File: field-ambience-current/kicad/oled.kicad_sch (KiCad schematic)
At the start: 7 parts, among them J1 USB_C_Receptacle (TYPE-C-31-M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

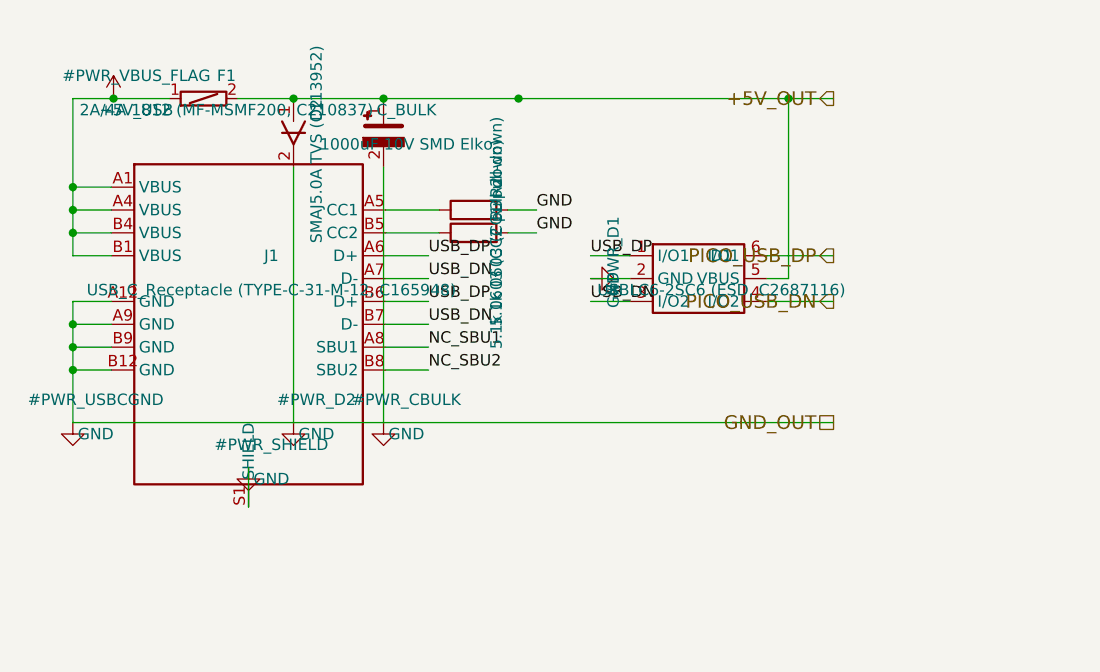
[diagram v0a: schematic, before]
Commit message: Add Sheet 3 (OLED) per SPEC v0.6 §6
J3 16-pin header für ER-OLEDM032-1W 256x64 SSD1322 OLED-Modul:
- Pin 1 VSS → GND
- Pin 2 VBAT → +5V mit lokalem C6b 10µF + C6c 100nF (250mA peak)
- Pin 3 VDD → +3V3 mit lokalem C6 100nF (Logic)
- Pin 4, 14-16 NC (Labels gegen Dangling-Wire-Warnings)
- Pin 5 BS1, Pin 6 BS0 → GND (4-wire SPI mode)
- Pin 7 RES#, Pin 8 CS#, Pin 9 DC# → OLED_RES/CS/DC (Pico GP9/5/8)
- Pin 10 E/RW, Pin 11 RW/E → GND (4-wire SPI unused)
- Pin 12 SCLK, Pin 13 SDIN → OLED_SCK/MOSI (Pico GP6/7)

Root sheet erweitert mit OLED sheet pin + inter-sheet SPI bus wires
zwischen Pico und OLED (SCK/MOSI/CS/DC/RES).

Generic Conn_01x16 lib_symbol generator added.

Analyzer: 0 errors, 30 warnings (down from 35), 20 components total.
All J3 pin_nets verified correct via analyzer pin_nets dump.
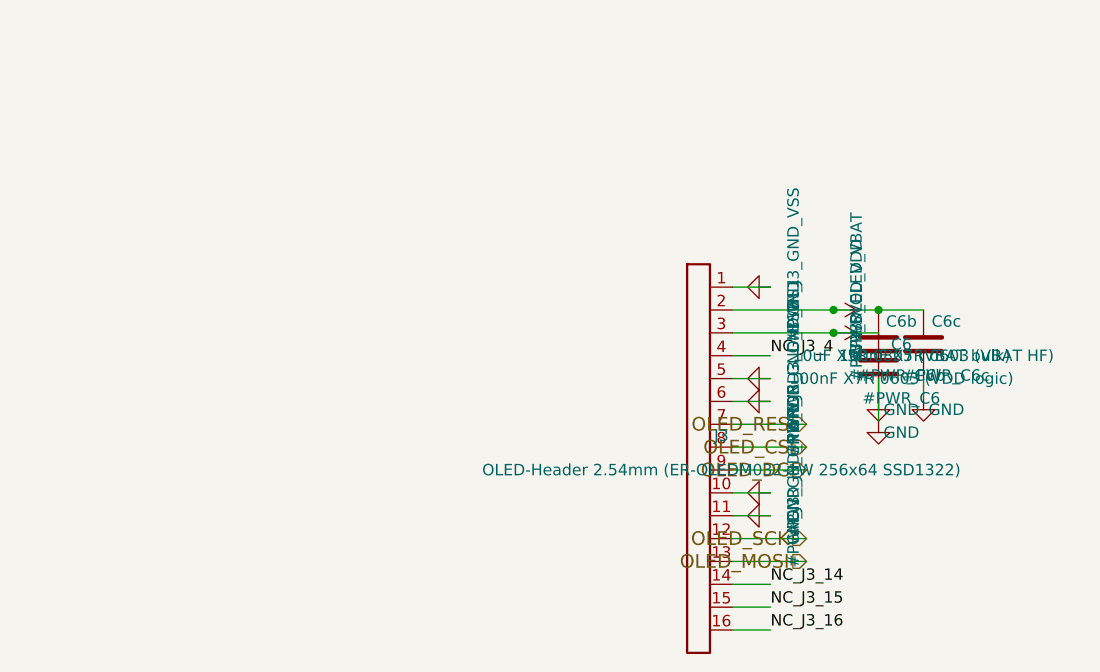
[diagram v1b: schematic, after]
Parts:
- removed C_BULK: 1000uF 10V SMD Elko, Capacitor_SMD:CP_Elec_8x6.7, symbol Device:CP
- removed D1: USBLC6-2SC6 (ESD, C2687116), Package_TO_SOT_SMD:SOT-23-6, symbol Power_Protection:USBLC6-2SC6
- removed D2: SMAJ5.0A TVS (C113952), Diode_SMD:D_SMA, symbol Device:D_TVS
- removed F1: 2A/4A 1812 (MF-MSMF200, C210837), Fuse:Fuse_1812_4532Metric, symbol Device:Polyfuse
- removed J1: USB_C_Receptacle (TYPE-C-31-M-12, C165948), Connector_USB:USB_C_Receptacle_HRO_TYPE-C-31-M-12, symbol Connector:USB_C_Receptacle
- removed R2: 5.1k 0603 (CC1 pull-down), Resistor_SMD:R_0603_1608Metric, symbol Device:R
- removed R3: 5.1k 0603 (CC2 pull-down), Resistor_SMD:R_0603_1608Metric, symbol Device:R
- added C6: 100nF X7R 0603 (VDD logic), Capacitor_SMD:C_0603_1608Metric, symbol Device:C
- added C6b: 10uF X5R 0805 (VBAT bulk), Capacitor_SMD:C_0805_2012Metric, symbol Device:C
- added C6c: 100nF X7R 0603 (VBAT HF), Capacitor_SMD:C_0603_1608Metric, symbol Device:C
- added J3: OLED-Header 2.54mm (ER-OLEDM032-1W 256x64 SSD1322), Connector_PinHeader_2.54mm:PinHeader_1x16_P2.54mm_Vertical, symbol Connector:Conn_01x16
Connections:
- net GND: now also C6.2, C6b.2, C6c.2, J3.1 (Pin_1), J3.10 (Pin_10), J3.11 (Pin_11), J3.5 (Pin_5), J3.6 (Pin_6)
- new net +3V3: C6.1, J3.3 (Pin_3)
- new net +5V: C6b.1, C6c.1, J3.2 (Pin_2)
- new net NC_J3_14: J3.14 (Pin_14)
- new net NC_J3_15: J3.15 (Pin_15)
- new net NC_J3_16: J3.16 (Pin_16)
- new net NC_J3_4: J3.4 (Pin_4)
- new net OLED_CS: J3.8 (Pin_8)
- new net OLED_DC: J3.9 (Pin_9)
- new net OLED_MOSI: J3.13 (Pin_13)
- new net OLED_RES: J3.7 (Pin_7)
- new net OLED_SCK: J3.12 (Pin_12)
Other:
- title: Field Ambience PCB — Sheet 1: Power Tree -> Field Ambience PCB — Sheet 3: OLED (ER-OLEDM032-1W)
